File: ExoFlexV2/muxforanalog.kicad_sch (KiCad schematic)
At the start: 2 parts

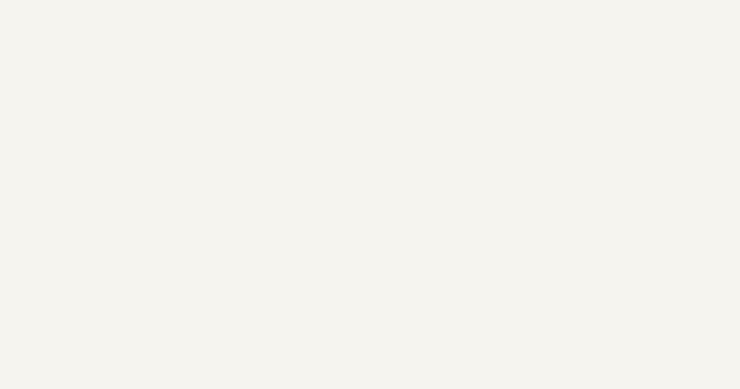
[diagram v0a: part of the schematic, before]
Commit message: Finalisation 1
- Ajout de pages pour la gestion des signaux négatif
- Modification des pages de torque et amplitude
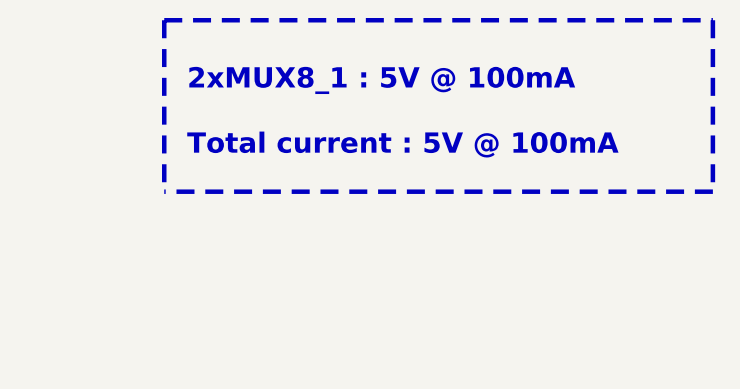
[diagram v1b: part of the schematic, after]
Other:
- note added: "2xMUX8_1 : 5V @ 100mA Total current : 5V @ 100mA"
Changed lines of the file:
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@@
     (stroke (width 0) (type default) (color 0 0 0 0))
+  )
+  (polyline (pts (xy 281.94 54.61) (xy 220.98 54.61))
+    (stroke (width 0.5) (type dash) (color 255 148 44 1))
   )
   (wire (pts (xy 162.56 101.6) (xy 156.21 101.6))
     (stroke (width 0) (type default) (color 0 0 0 0))
+  )
+  (polyline (pts (xy 220.98 35.56) (xy 220.98 54.61))
+    (stroke (width 0.5) (type dash) (color 255 148 44 1))
   )
   (wire (pts (xy 162.56 59.69) (xy 156.21 59.69))
@@
     (stroke (width 0) (type default) (color 0 0 0 0))
   )
+  (polyline (pts (xy 281.94 35.56) (xy 281.94 54.61))
+    (stroke (width 0.5) (type dash) (color 255 148 44 1))
+  )
   (wire (pts (xy 135.89 90.17) (xy 162.56 90.17))
     (stroke (width 0) (type default) (color 0 0 0 0))
@@
   (wire (pts (xy 102.87 59.69) (xy 102.87 101.6))
     (stroke (width 0) (type default) (color 0 0 0 0))
+  )
+  (polyline (pts (xy 220.98 35.56) (xy 281.94 35.56))
+    (stroke (width 0.5) (type dash) (color 255 148 44 1))
   )
   (wire (pts (xy 100.33 62.23) (xy 135.89 62.23))
@@
     (stroke (width 0) (type default) (color 0 0 0 0))
   )
+  (text "2xMUX8_1 : 5V @ 100mA\n\nTotal current : 5V @ 100mA" (at 223.52 50.8 0)
+    (effects (font (size 2.25 2.25) (thickness 0.5) bold) (justify left bottom))
+  )
   (global_label "ANA_LIM_DATA" (shape input) (at 156.21 111.76 0) (fields_autoplaced)
